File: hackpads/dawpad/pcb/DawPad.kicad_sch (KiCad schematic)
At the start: 0 parts

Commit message: Connect inputs on the DawPad schematic and lay things out on the PCB
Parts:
- added D1, D10, D11, D12, D2, D3, D4, D5, D6, D7, D8, D9: D, Diode_THT:D_DO-35_SOD27_P7.62mm_Horizontal, symbol Device:D
- added R1, R2: 4.7k, Resistor_THT:R_Axial_DIN0204_L3.6mm_D1.6mm_P7.62mm_Horizontal, symbol Device:R
- added SW1, SW10, SW11, SW12, SW2, SW3, SW4, SW5, SW6, SW7, SW8, SW9: SW_Push, Button_Switch_Keyboard:SW_Cherry_MX_1.00u_PCB, symbol Switch:SW_Push
- added SW13, SW14, SW15, SW16: RotaryEncoder_Switch_MP, Rotary_Encoder:RotaryEncoder_Alps_EC11E-Switch_Vertical_H20mm, symbol Device:RotaryEncoder_Switch_MP
- added U1: XIAO-RP2040-DIP, Seeed Studio XIAO Series Library:XIAO-RP2040-DIP, symbol Seeed Studio XIAO Series:XIAO-RP2040-DIP
- added U2: MCP23017_SO, Package_SO:SOIC-28W_7.5x17.9mm_P1.27mm, symbol Interface_Expansion:MCP23017_SO
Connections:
- new net: D1.2 (A), SW1.1
- new net: U1.1 (GPIO26/ADC0/A0), U2.20 (INTA)
- new net: U1.2 (GPIO27/ADC1/A1), U2.19 (INTB)
- new net: D5.2 (A), SW6.1
- new net: D12.2 (A), SW12.1
- new net: D11.2 (A), SW11.1
- new net: D7.2 (A), SW9.1
- new net: D10.2 (A), SW8.1
- new net: D8.2 (A), SW4.1
- new net: D3.2 (A), SW3.1
- new net: D4.2 (A), SW5.1
- new net: D2.2 (A), SW2.1
- new net: D6.2 (A), SW7.1
- new net: D9.2 (A), SW10.1
- new net +3V3: R1.1, R2.1, U1.12 (3V3), U2.18 (~{RESET}), U2.9 (VDD)
- new net +5V: U1.14 (VBUS)
- new net COL-0: SW1.2, SW5.2, SW9.2, U2.24 (GPA3)
- new net COL-1: SW10.2, SW2.2, SW6.2, U2.25 (GPA4)
- new net COL-2: SW11.2, SW3.2, SW7.2, U2.26 (GPA5)
- new net COL-3: SW12.2, SW4.2, SW8.2, U2.27 (GPA6)
- new net ENC1_A: SW13.A, U2.1 (GPB0)
- new net ENC1_B: SW13.B, U2.2 (GPB1)
- new net ENC1_SW: SW13.S1, U1.11 (GPIO3/MOSI)
- new net ENC2_A: SW14.A, U2.3 (GPB2)
- new net ENC2_B: SW14.B, U2.4 (GPB3)
- new net ENC2_SW: SW14.S1, U1.10 (GPIO4/MISO)
- new net ENC3_A: SW15.A, U2.5 (GPB4)
- new net ENC3_B: SW15.B, U2.6 (GPB5)
- new net ENC3_SW: SW15.S1, U1.9 (GPIO2/SCK)
- new net ENC4_A: SW16.A, U2.7 (GPB6)
- new net ENC4_B: SW16.B, U2.8 (GPB7)
- new net ENC4_SW: SW16.S1, U1.8 (GPIO1/RX)
- new net GND: SW13.C, SW13.MP, SW13.S2, SW14.C, SW14.MP, SW14.S2, SW15.C, SW15.MP, SW15.S2, SW16.C, SW16.MP, SW16.S2, U1.13 (GND), U2.10 (VSS), U2.15 (A0), U2.16 (A1), U2.17 (A2)
- new net ROW-0: D1.1 (K), D2.1 (K), D3.1 (K), D8.1 (K), U2.21 (GPA0)
- new net ROW-1: D10.1 (K), D4.1 (K), D5.1 (K), D6.1 (K), U2.22 (GPA1)
- new net ROW-2: D11.1 (K), D12.1 (K), D7.1 (K), D9.1 (K), U2.23 (GPA2)
- new net SCL: R2.2, U1.6 (GPIO7/SCL), U2.12 (SCK)
- new net SDA: R1.2, U1.5 (GPIO6/SDA), U2.13 (SDA)
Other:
- note added: "I2C Pull-ups"

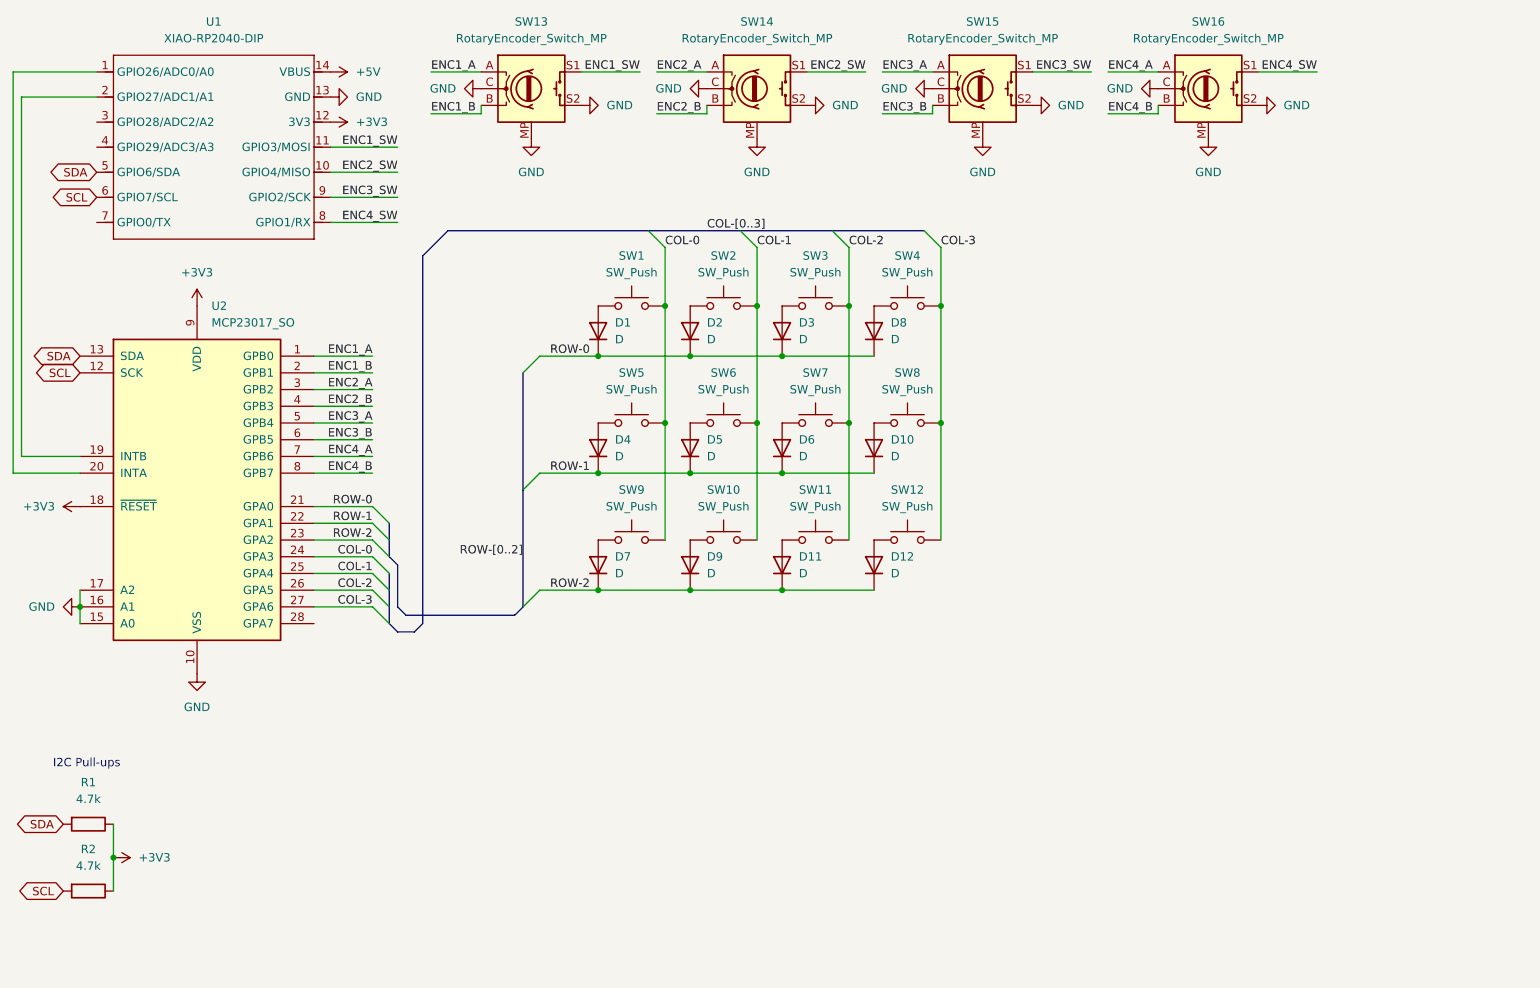
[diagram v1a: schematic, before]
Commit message: Add LEDs to and finish PCB for DawPad
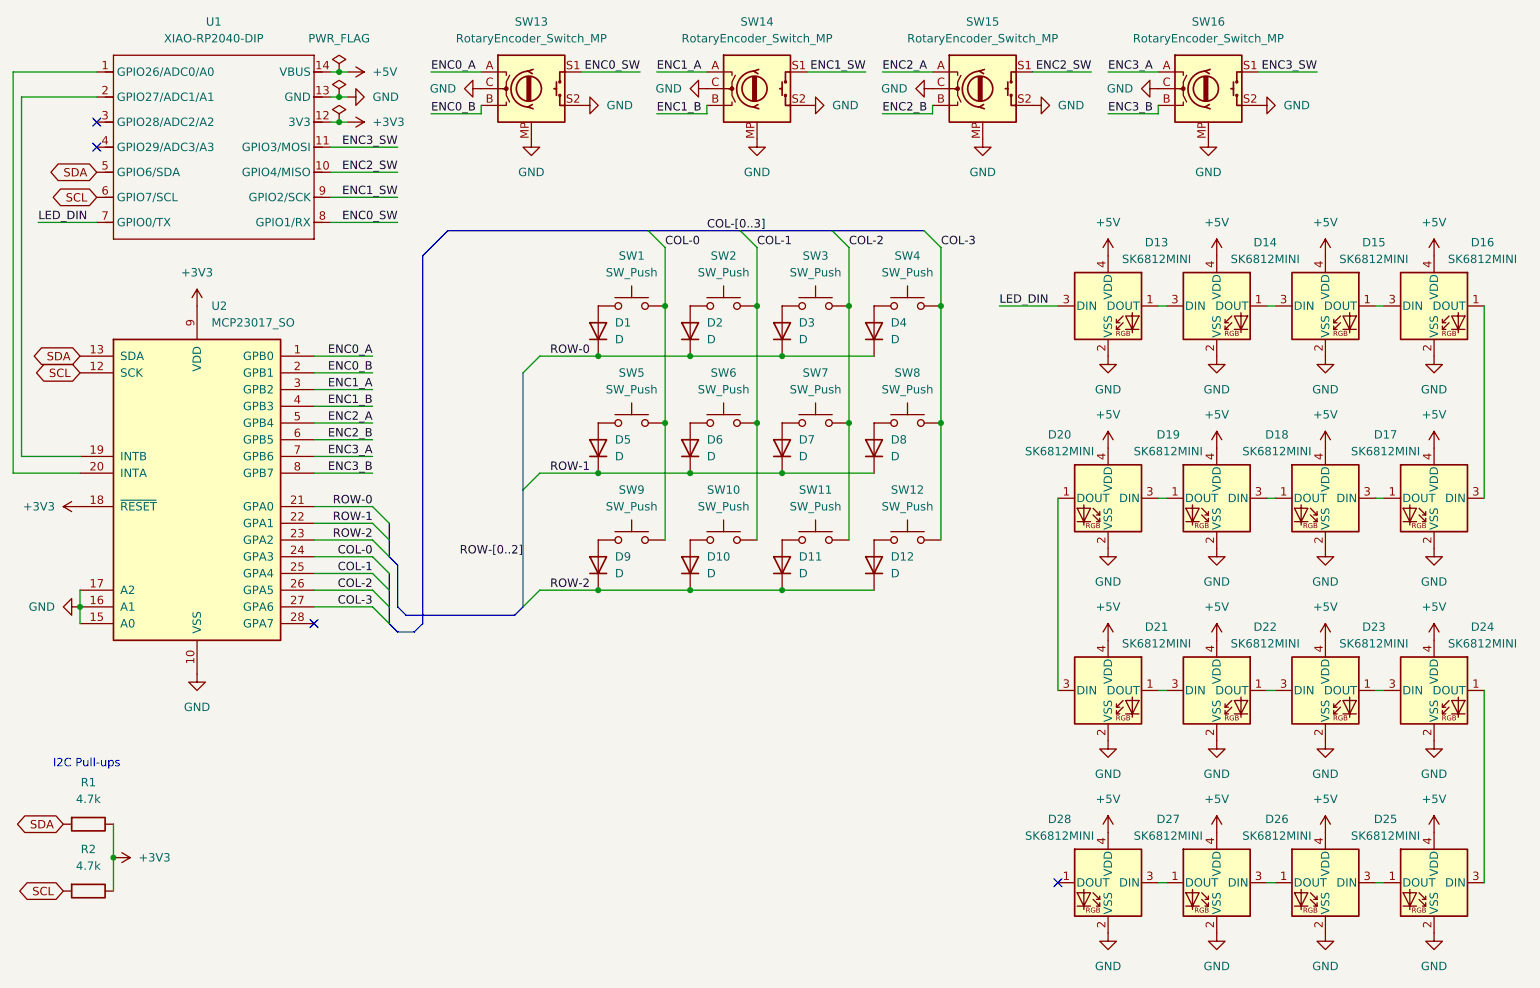
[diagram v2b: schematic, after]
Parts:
- added D13, D14, D15, D16: SK6812MINI, LED_SMD:LED_SK6812MINI_PLCC4_3.5x3.5mm_P1.75mm, symbol LED:SK6812MINI
- added D17, D18, D19, D20, D21, D22, D23, D24, D25, D26, D27, D28: SK6812MINI, SK6812MINI-E:SK6812MINI-E, symbol LED:SK6812MINI
- renumbered D9 to D10, D8 to D4, D4 to D5, D5 to D6, D6 to D7, D10 to D8, D7 to D9
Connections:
- net ENC4_A is gone; now on net ENC3_A: SW16.A, U2.7 (GPB6)
- net ENC4_B is gone; now on net ENC3_B: SW16.B, U2.8 (GPB7)
- net +5V: now also D13.4 (VDD), D14.4 (VDD), D15.4 (VDD), D16.4 (VDD), D17.4 (VDD), D18.4 (VDD), D19.4 (VDD), D20.4 (VDD), D21.4 (VDD), D22.4 (VDD), D23.4 (VDD), D24.4 (VDD), D25.4 (VDD), D26.4 (VDD), D27.4 (VDD), D28.4 (VDD)
- net ENC1_A: now also SW14.A, U2.3 (GPB2); no longer SW13.A, U2.1 (GPB0)
- net ENC1_B: now also SW14.B, U2.4 (GPB3); no longer SW13.B, U2.2 (GPB1)
- net ENC1_SW: now also SW14.S1, U1.9 (GPIO2/SCK); no longer SW13.S1, U1.11 (GPIO3/MOSI)
- net ENC2_A: now also SW15.A, U2.5 (GPB4); no longer SW14.A, U2.3 (GPB2)
- net ENC2_B: now also SW15.B, U2.6 (GPB5); no longer SW14.B, U2.4 (GPB3)
- net ENC2_SW: now also SW15.S1; no longer SW14.S1
- net ENC3_A: no longer SW15.A, U2.5 (GPB4)
- net ENC3_B: no longer SW15.B, U2.6 (GPB5)
- net ENC3_SW: now also SW16.S1, U1.11 (GPIO3/MOSI); no longer SW15.S1, U1.9 (GPIO2/SCK)
- net GND: now also D13.2 (VSS), D14.2 (VSS), D15.2 (VSS), D16.2 (VSS), D17.2 (VSS), D18.2 (VSS), D19.2 (VSS), D20.2 (VSS), D21.2 (VSS), D22.2 (VSS), D23.2 (VSS), D24.2 (VSS), D25.2 (VSS), D26.2 (VSS), D27.2 (VSS), D28.2 (VSS)
- net LED_DIN: now reaches U1.7 (GPIO0/TX)
- net LED_DIN: now also D13.3 (DIN)
- net ENC4_SW renamed ENC0_SW
- net ENC0_SW: now also SW13.S1; no longer SW16.S1
- new net: D26.1 (DOUT), D27.3 (DIN)
- new net: D25.1 (DOUT), D26.3 (DIN)
- new net: D27.1 (DOUT), D28.3 (DIN)
- new net: D17.1 (DOUT), D18.3 (DIN)
- new net: D16.1 (DOUT), D17.3 (DIN)
- new net: D14.1 (DOUT), D15.3 (DIN)
- new net: D13.1 (DOUT), D14.3 (DIN)
- new net: D21.1 (DOUT), D22.3 (DIN)
- new net: D20.1 (DOUT), D21.3 (DIN)
- new net: D23.1 (DOUT), D24.3 (DIN)
- new net: D22.1 (DOUT), D23.3 (DIN)
- new net: D19.1 (DOUT), D20.3 (DIN)
- new net: D18.1 (DOUT), D19.3 (DIN)
- new net: D24.1 (DOUT), D25.3 (DIN)
- new net: D15.1 (DOUT), D16.3 (DIN)
- new net ENC0_A: SW13.A, U2.1 (GPB0)
- new net ENC0_B: SW13.B, U2.2 (GPB1)
- no-connect marks 0 -> 4
